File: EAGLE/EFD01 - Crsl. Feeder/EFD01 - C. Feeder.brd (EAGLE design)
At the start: 50 x 50 mm, 34 parts, among them J1 MOD TOOL, J2 SPI, J3 MOT, J4 FTDI, Q1 BSS138, Q2 16MHz, U1 SP3485, U2 TCST1030, U3 ATMEGA238, U4 DRV8825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

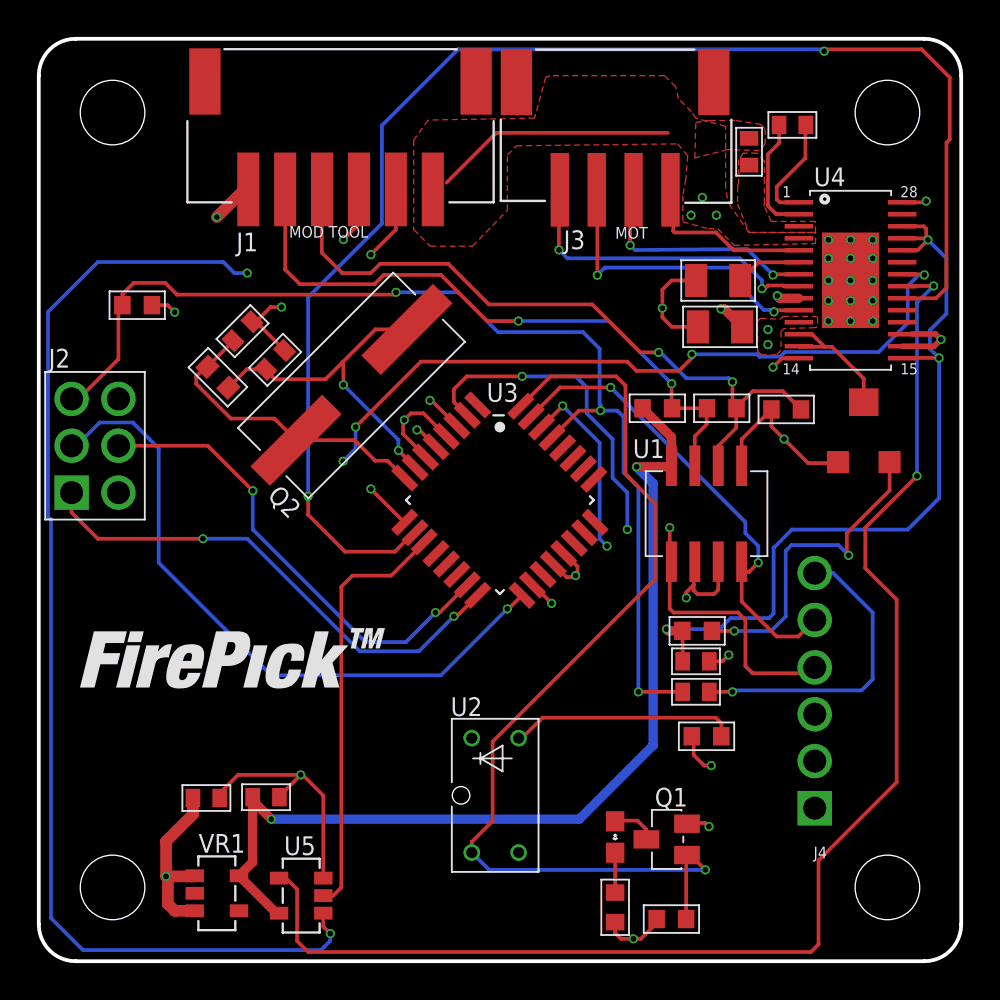
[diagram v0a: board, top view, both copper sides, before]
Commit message: Made some simple adjustments (moved traces, increased width on current carrying components).  Added P/N and TW logo.  Generated gerbers for Rev--.
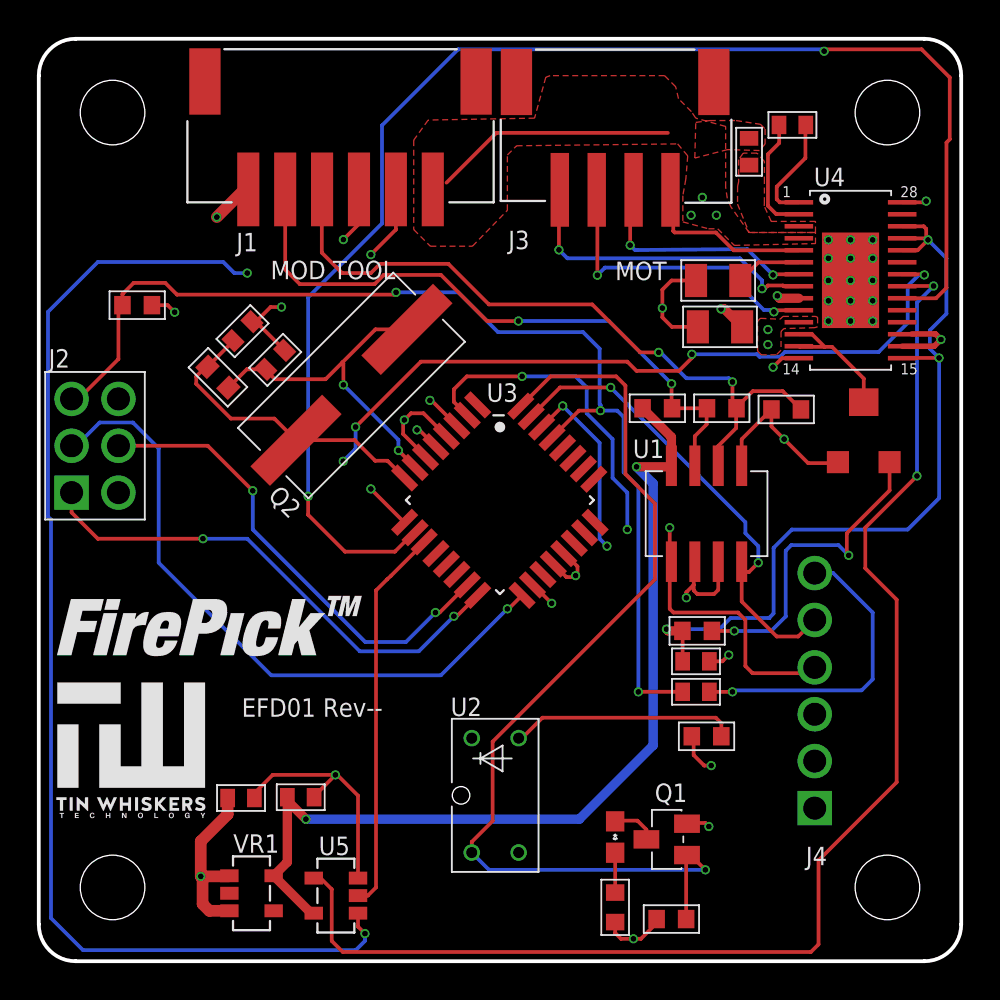
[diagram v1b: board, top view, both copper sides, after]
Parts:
- added U$1: TIN-WHISKERSSMALL, !tin-whiskers-logo:TIN-WHISKERS-SMALL
- moved LOGO2 2.15 mm to (0.79, 14.8)
- moved C7 1.88 mm to (11.0, 8.85)
- moved C8 1.88 mm to (14.2, 8.89)
- moved U5 1.88 mm to (16.1, 3.56)
- moved VR1 1.88 mm to (11.5, 3.68)
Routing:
- net !ENBL_AVR: track 23.0 -> 21.0 mm
- net !ENBL_MOD: track 74.0 -> 75.9 mm
- net +3V3: track 52.7 -> 50.8 mm
- net !ENABLE: track 74.1 -> 72.2 mm
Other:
- board text added: "EFD01 Rev--"

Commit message: BOMs finished, inventory sheet created.
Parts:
- R2: value 100R -> 120R
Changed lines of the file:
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@@
 <attribute name="NAME" x="3.855" y="36.487" size="1" layer="51" font="vector" ratio="11"/>
 </element>
-<element name="R2" library="TinWhiskers" package="R0603" value="100R" x="37.0205" y="29.972" smashed="yes" rot="R180">
+<element name="R2" library="TinWhiskers" package="R0603" value="120R" x="37.0205" y="29.972" smashed="yes" rot="R180">
 <attribute name="PARTNO" value="RC0603FR-07100RL" x="37.0205" y="29.972" size="1.778" layer="27" rot="R180" display="off"/>
 <attribute name="NAME" x="35.5415" y="30.8482" size="1" layer="51" font="vector" ratio="11"/>
